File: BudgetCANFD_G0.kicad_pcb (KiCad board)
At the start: 2 copper layers, 66 x 33 mm, 87 parts, among them IC1 STM32G0B1KET6, IC2 M74VHC1GT66DTT1G, IC3 TJA1021TK_20_C,118, IC4 TPS56428DDA, IC5 NCV7356D1R2G, IC6 M74VHC1GT66DTT1G, J1 USB_C_Receptacle_USB2.0, J2 DB9_Male_MountingHoles, J3 20021511-00014T4LF, J4 Conn_01x02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

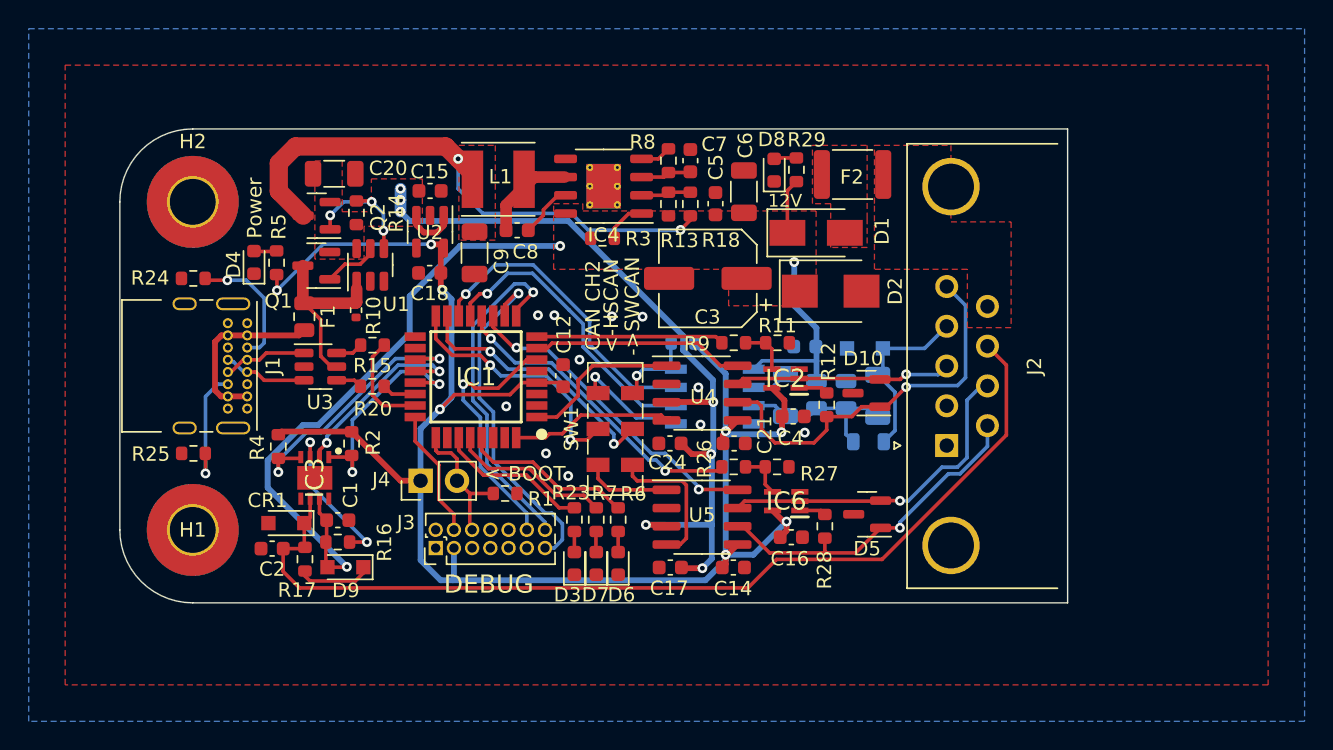
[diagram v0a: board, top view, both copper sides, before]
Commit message: Update to v1.1
Add support for an external clock if needed in the future
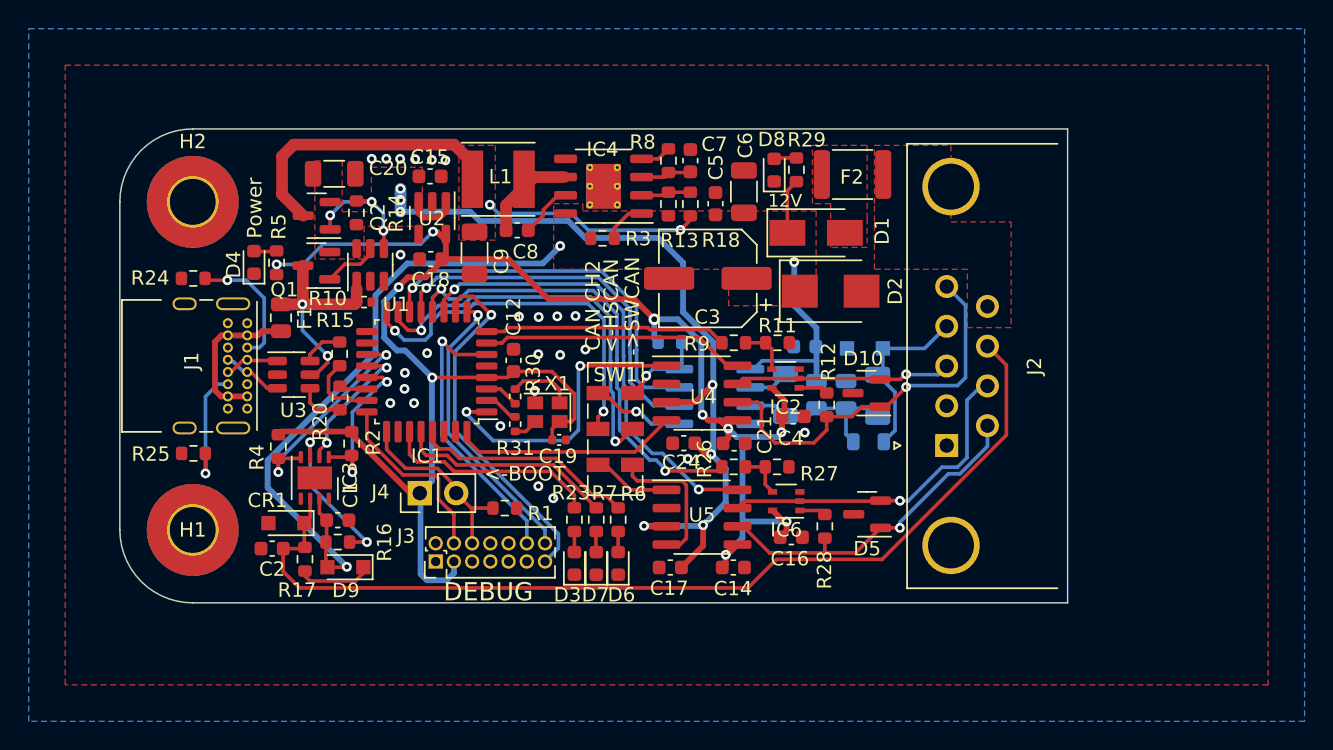
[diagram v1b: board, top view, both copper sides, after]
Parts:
- added C19: 0.1uF, Capacitor_SMD:C_0402_1005Metric, F.Cu at (143.6, 102.3)
- added R30: 0R, Resistor_SMD:R_0402_1005Metric, F.Cu at (140.6, 99.3)
- added R31: 0R, Resistor_SMD:R_0402_1005Metric, F.Cu at (140.6, 101.2)
- added X1: SG-210STF, Oscillator:Oscillator_SMD_SeikoEpson_SG210-4Pin_2.5x2.0mm, F.Cu at (142.8, 100.4)
- IC1: footprint SamacSys_Parts:QFP80P900X900X160-32N -> Package_QFP:LQFP-32_7x7mm_P0.8mm
- IC2, IC6: footprint SamacSys_Parts:SOT65P210X110-5N -> Package_TO_SOT_SMD:SOT-353_SC-70-5
- IC3: footprint SamacSys_Parts:SON65P300X300X100-9N-D -> Package_SON:HVSON-8-1EP_3x3mm_P0.65mm_EP1.6x2.4mm
- IC5: footprint SamacSys_Parts:SOIC127P600X172-8N -> Package_SO:SOIC-8_3.9x4.9mm_P1.27mm
- moved C12 3.62 mm to (140.5, 96.8)
- moved IC1 3.45 mm to (134.4, 97.6)
- moved R20 2.39 mm to (128.4, 99.4), turned to 90 degrees
- moved R15 2.37 mm to (128.3, 96.3), turned to 90 degrees
- moved U3 1.94 mm to (125.1, 97.8)
- moved F1 1.63 mm to (124.3, 93.8)
- moved R1 1.02 mm to (139.9, 107.1)
- moved C15 1.02 mm to (134.6, 83.9)
- moved U2 0.98 mm to (134.8, 86.8)
- moved C18 0.97 mm to (134.7, 89.7)
- moved C24 0.96 mm to (152.3, 102.5)
- moved J3 0.94 mm to (135.0, 110.8)
- moved R19 0.92 mm to (151.4, 95.5), turned to 180 degrees
- moved J4 0.87 mm to (133.9, 106.0)
- moved R10 0.79 mm to (130.0, 92.7), turned to 0 degrees
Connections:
- IC1 pad 2: unconnected-(IC1-Pad2) -> STM32_OSC_IN
- IC1 pad 3: unconnected-(IC1-Pad3) -> STM32_OSC_EN
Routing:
- net FDCAN2_TERM_EN: track 21.9 -> 32.1 mm
- net FDCAN1_TX: track 11.1 -> 21.0 mm, vias 0 -> 2
- net FDCAN2_SLEEP_EN: track 22.6 -> 32.3 mm
- net +3V3: track 118.2 -> 127.8 mm, vias 8 -> 10
- net FDCAN2_RX: track 18.4 -> 27.9 mm
- net FDCAN2_TX: track 17.8 -> 26.2 mm
- net SWCAN_M0: track 20.8 -> 26.2 mm
- net SWCAN_M1: track 21.7 -> 26.9 mm
- net LED_3: track 10.5 -> 15.1 mm
- net Net-(R30-Pad1): track 0.00 -> 4.51 mm
- net FDCAN1_RX: track 11.3 -> 15.7 mm
- net LIN1_RX: track 16.0 -> 11.8 mm
- net SWDIO: track 8.98 -> 13.0 mm
- net LIN1_TX: track 19.3 -> 15.3 mm
- net BUCK_5V: track 39.2 -> 35.3 mm
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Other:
- board text added: "BudgetCANFD v1.1"
- board text removed: "BudgetCANFD v1.0"

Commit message: Update BOM
Update part numbers for LCSC parts
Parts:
- C7: value 0.47uF -> 4.7nF
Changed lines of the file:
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@@
     (tags "capacitor")
     (property "Digi-Key_PN" "587-3328-1-ND")
-    (property "LCSC Part #" "C12891")
+    (property "LCSC Part #" "C90146")
     (property "Manufacturer_Part_Number" "EMK316ABJ226ML-T")
     (property "Sheetfile" "BudgetCANFD_G0.kicad_sch")
@@
     (tags "capacitor")
     (property "Digi-Key_PN" "587-3328-1-ND")
-    (property "LCSC Part #" "C12891")
+    (property "LCSC Part #" "C90146")
     (property "Manufacturer_Part_Number" "EMK316ABJ226ML-T")
     (property "Sheetfile" "BudgetCANFD_G0.kicad_sch")
@@
     (tags "SOD-323")
     (property "Digi-Key_PN" "1727-1225-1-ND")
-    (property "LCSC Part #" "C2831530")
+    (property "LCSC Part #" "C58901")
     (property "Manufacturer_Part_Number" "PESD1LIN,135")
     (property "Sheetfile" "BudgetCANFD_G0.kicad_sch")
@@
     (tags "capacitor")
     (property "Digi-Key_PN" "445-5810-1-ND")
-    (property "LCSC Part #" "C2167812")
+    (property "LCSC Part #" "C53987")
     (property "Manufacturer_Part_Number" "CGA3E2X7R2A472K080AA")
     (property "Sheetfile" "BudgetCANFD_G0.kicad_sch")
@@
       (effects (font (size 1 1) (thickness 0.15)))
     )
-    (fp_text value "0.47uF" (at 0 1.43 90) (layer "F.Fab")
+    (fp_text value "4.7nF" (at 0 1.43 90) (layer "F.Fab")
       (effects (font (size 1 1) (thickness 0.15)))
     )
@@
     (descr "Resistor SMD 0402 (1005 Metric), square (rectangular) end terminal, IPC_7351 nominal, (Body size source: IPC-SM-782 page 72, https://www.pcb-3d.com/wordpress/wp-content/uploads/ipc-sm-782a_amendment_1_and_2.pdf), generated with kicad-footprint-generator")
     (tags "resistor")
+    (property "Digi-Key_PN" "CR0402AJ/-000GASCT-ND")
+    (property "LCSC Part #" "C60490")
     (property "Sheetfile" "BudgetCANFD_G0.kicad_sch")
     (property "Sheetname" "")
@@
     (property "Digi-Key_PN" "296-24277-1-ND")
     (property "Height" "1.1")
-    (property "LCSC Part #" "C2673183")
+    (property "LCSC Part #" "C2762292")
     (property "Manufacturer_Name" "Texas Instruments")
     (property "Manufacturer_Part_Number" "SN74LVC1G66QDCKRQ1")
@@
     (descr "Capacitor SMD 0402 (1005 Metric), square (rectangular) end terminal, IPC_7351 nominal, (Body size source: IPC-SM-782 page 76, https://www.pcb-3d.com/wordpress/wp-content/uploads/ipc-sm-782a_amendment_1_and_2.pdf), generated with kicad-footprint-generator")
     (tags "capacitor")
-    (property "Digi-Key_PN" "311-1417-1-ND")
-    (property "LCSC Part #" "C1554")
-    (property "Manufacturer_Part_Number" "CC0402JRNPO9BN200")
+    (property "Digi-Key_PN" "1276-1002-1-ND")
+    (property "LCSC Part #" "C41851")
+    (property "Manufacturer_Part_Number" "")
     (property "Sheetfile" "BudgetCANFD_G0.kicad_sch")
     (property "Sheetname" "")
@@
     (property "Digi-Key_PN" "296-24277-1-ND")
     (property "Height" "1.1")
-    (property "LCSC Part #" "C2673183")
+    (property "LCSC Part #" "C2762292")
     (property "Manufacturer_Name" "Texas Instruments")
     (property "Manufacturer_Part_Number" "SN74LVC1G66QDCKRQ1")
@@
     (descr "SMD Crystal Oscillator Seiko Epson SG-210 https://support.epson.biz/td/api/doc_check.php?mode=dl&lang=en&Parts=SG-210SED, 2.5x2.0mm^2 package")
     (tags "SMD SMT crystal oscillator")
+    (property "Digi-Key_PN" "50-ECS-2520MVLC-080-BN-CT-ND")
+    (property "LCSC Part #" "C717682")
     (property "Sheetfile" "BudgetCANFD_G0.kicad_sch")
     (property "Sheetname" "")
@@
     (descr "Resistor SMD 0402 (1005 Metric), square (rectangular) end terminal, IPC_7351 nominal, (Body size source: IPC-SM-782 page 72, https://www.pcb-3d.com/wordpress/wp-content/uploads/ipc-sm-782a_amendment_1_and_2.pdf), generated with kicad-footprint-generator")
     (tags "resistor")
+    (property "Digi-Key_PN" "CR0402AJ/-000GASCT-ND")
+    (property "LCSC Part #" "C60490")
     (property "Sheetfile" "BudgetCANFD_G0.kicad_sch")
     (property "Sheetname" "")
@@
     (tags "SOD-323")
     (property "Digi-Key_PN" "1727-1225-1-ND")
-    (property "LCSC Part #" "C2831530")
+    (property "LCSC Part #" "C58901")
     (property "Manufacturer_Part_Number" "PESD1LIN,135")
     (property "Sheetfile" "BudgetCANFD_G0.kicad_sch")
